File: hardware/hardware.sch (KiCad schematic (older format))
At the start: 8 parts

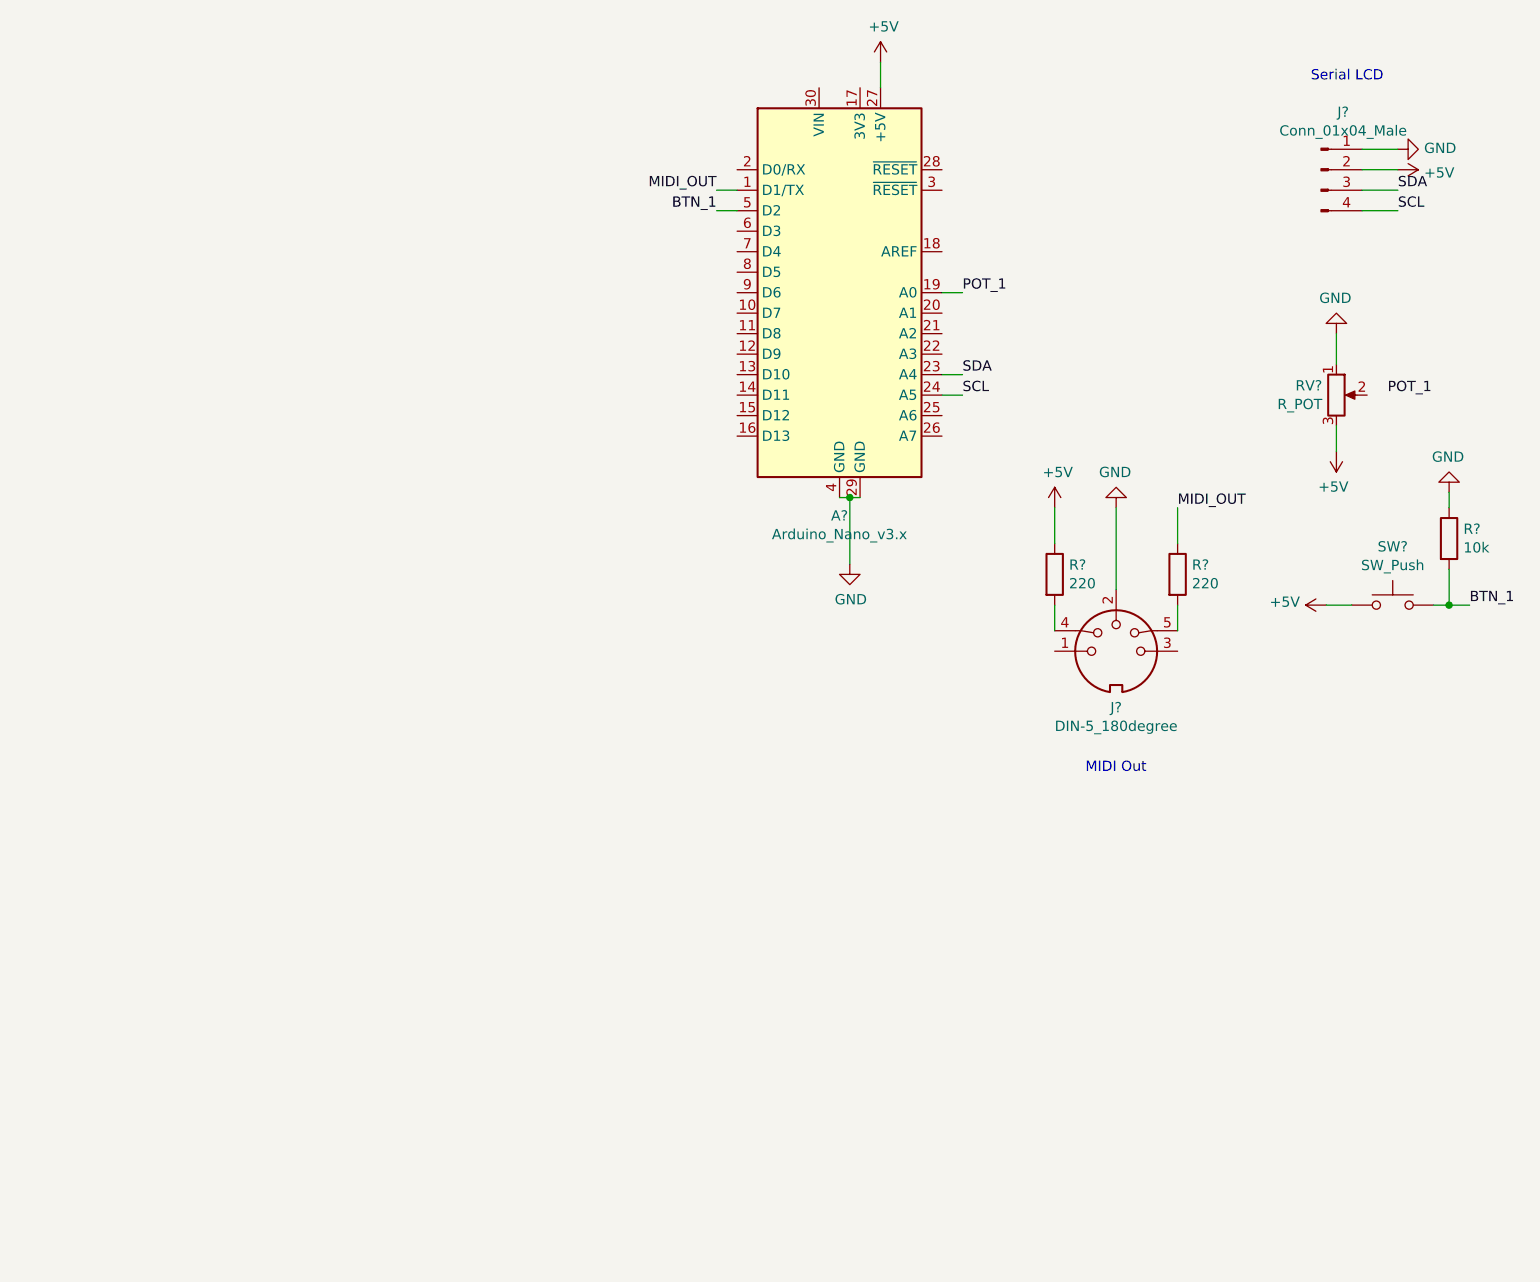
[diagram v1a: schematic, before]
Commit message: update schematic and add todo
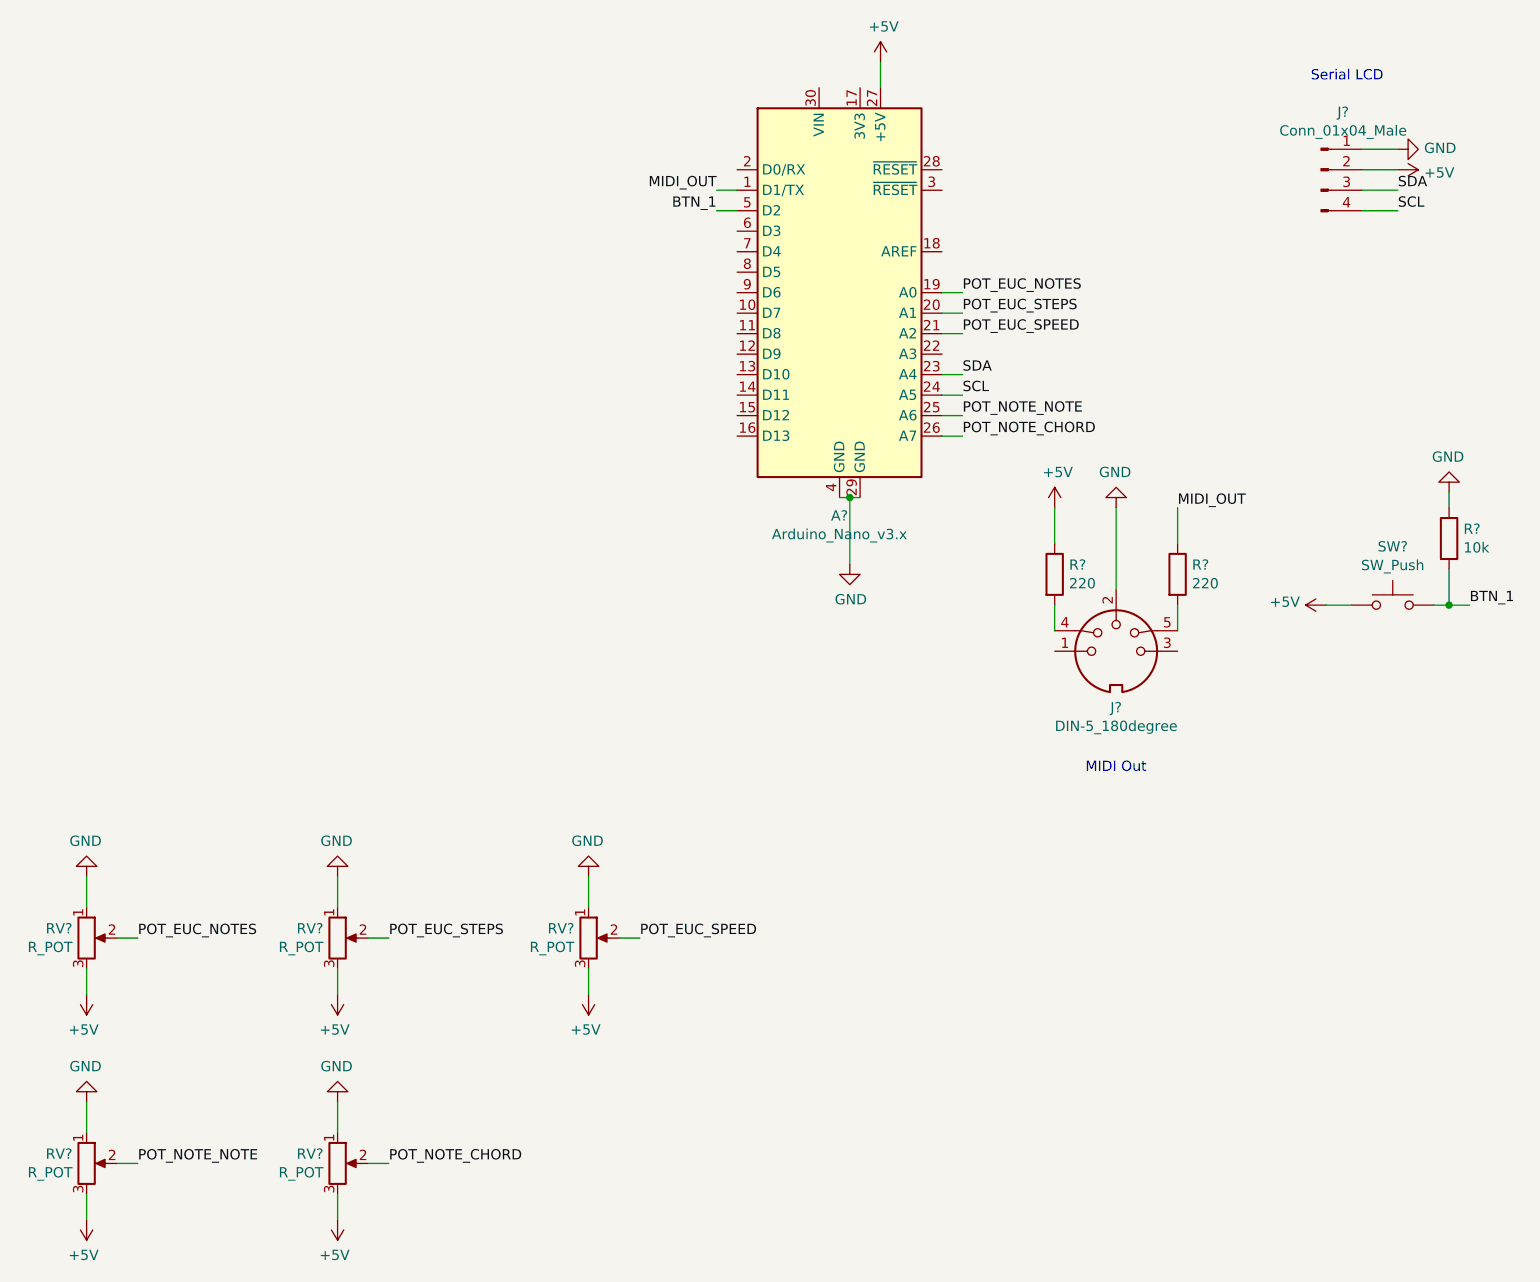
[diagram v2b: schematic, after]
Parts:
- added RV? (x4): R_POT, symbol Device:R_POT
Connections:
- net POT_1 is gone; now on net POT_EUC_NOTES: A?.19 (A0)
- net +5V: now also RV?.3, RV?.3, RV?.3, RV?.3
- net GND: now also RV?.1, RV?.1, RV?.1, RV?.1
- net POT_EUC_STEPS: now reaches A?.20 (A1)
- net POT_EUC_STEPS: now also RV?.2
- net POT_EUC_SPEED: now reaches A?.21 (A2)
- net POT_EUC_SPEED: now also RV?.2
- net POT_NOTE_NOTE: now reaches A?.25 (A6)
- net POT_NOTE_NOTE: now also RV?.2
- net POT_NOTE_CHORD: now reaches A?.26 (A7)
- net POT_NOTE_CHORD: now also RV?.2
- net POT_EUC_NOTES: now reaches RV?.2
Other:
- moved on the sheet: RV?
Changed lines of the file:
@@
 L Device:R_POT RV?
 U 1 1 5FC51EFD
-P 7500 3250
-F 0 "RV?" H 7431 3296 50  0000 R CNN
-F 1 "R_POT" H 7431 3205 50  0000 R CNN
-F 2 "" H 7500 3250 50  0001 C CNN
-F 3 "~" H 7500 3250 50  0001 C CNN
-	1    7500 3250
+P 1400 5900
+F 0 "RV?" H 1331 5946 50  0000 R CNN
+F 1 "R_POT" H 1331 5855 50  0000 R CNN
+F 2 "" H 1400 5900 50  0001 C CNN
+F 3 "~" H 1400 5900 50  0001 C CNN
+	1    1400 5900
 	1    0    0    -1
 $EndComp
@@
 	4475 2250 4575 2250
 Text Label 5675 2750 0    50   ~ 0
-POT_1
+POT_EUC_NOTES
 Text Label 4475 2350 2    50   ~ 0
 BTN_1
@@
 L power:GND #PWR?
 U 1 1 5FC5C0D4
-P 7500 2950
-F 0 "#PWR?" H 7500 2700 50  0001 C CNN
-F 1 "GND" H 7505 2777 50  0000 C CNN
-F 2 "" H 7500 2950 50  0001 C CNN
-F 3 "" H 7500 2950 50  0001 C CNN
-	1    7500 2950
+P 1400 5600
+F 0 "#PWR?" H 1400 5350 50  0001 C CNN
+F 1 "GND" H 1405 5427 50  0000 C CNN
+F 2 "" H 1400 5600 50  0001 C CNN
+F 3 "" H 1400 5600 50  0001 C CNN
+	1    1400 5600
 	-1   0    0    1
 $EndComp
@@
 L power:+5V #PWR?
 U 1 1 5FC5C2F2
-P 7500 3525
-F 0 "#PWR?" H 7500 3375 50  0001 C CNN
-F 1 "+5V" H 7515 3698 50  0000 C CNN
-F 2 "" H 7500 3525 50  0001 C CNN
-F 3 "" H 7500 3525 50  0001 C CNN
-	1    7500 3525
-	-1   0    0    1
-$EndComp
-Wire Wire Line
-	7500 2950 7500 3100
-Wire Wire Line
-	7500 3400 7500 3525
-Text Label 7750 3250 0    50   ~ 0
-POT_1
+P 1400 6175
+F 0 "#PWR?" H 1400 6025 50  0001 C CNN
+F 1 "+5V" H 1415 6348 50  0000 C CNN
+F 2 "" H 1400 6175 50  0001 C CNN
+F 3 "" H 1400 6175 50  0001 C CNN
+	1    1400 6175
+	-1   0    0    1
+$EndComp
+Wire Wire Line
+	1400 5600 1400 5750
+Wire Wire Line
+	1400 6050 1400 6175
+Text Label 1650 5900 0    50   ~ 0
+POT_EUC_NOTES
 Text Label 8150 4275 0    50   ~ 0
 BTN_1
@@
 Wire Wire Line
 	8050 4275 8150 4275
+$Comp
+L Device:R_POT RV?
+U 1 1 5FCA6913
+P 2625 5900
+F 0 "RV?" H 2556 5946 50  0000 R CNN
+F 1 "R_POT" H 2556 5855 50  0000 R CNN
+F 2 "" H 2625 5900 50  0001 C CNN
+F 3 "~" H 2625 5900 50  0001 C CNN
+	1    2625 5900
+	1    0    0    -1
+$EndComp
+$Comp
+L power:GND #PWR?
+U 1 1 5FCA6919
+P 2625 5600
+F 0 "#PWR?" H 2625 5350 50  0001 C CNN
+F 1 "GND" H 2630 5427 50  0000 C CNN
+F 2 "" H 2625 5600 50  0001 C CNN
+F 3 "" H 2625 5600 50  0001 C CNN
+	1    2625 5600
+	-1   0    0    1
+$EndComp
+$Comp
+L power:+5V #PWR?
+U 1 1 5FCA691F
+P 2625 6175
+F 0 "#PWR?" H 2625 6025 50  0001 C CNN
+F 1 "+5V" H 2640 6348 50  0000 C CNN
+F 2 "" H 2625 6175 50  0001 C CNN
+F 3 "" H 2625 6175 50  0001 C CNN
+	1    2625 6175
+	-1   0    0    1
+$EndComp
+Wire Wire Line
+	2625 5600 2625 5750
+Wire Wire Line
+	2625 6050 2625 6175
+Text Label 2875 5900 0    50   ~ 0
+POT_EUC_STEPS
+Text Label 5675 2850 0    50   ~ 0
+POT_EUC_STEPS
+Wire Wire Line
+	5675 2850 5575 2850
+$Comp
+L Device:R_POT RV?
+U 1 1 5FCA7C9D
+P 3850 5900
+F 0 "RV?" H 3781 5946 50  0000 R CNN
+F 1 "R_POT" H 3781 5855 50  0000 R CNN
+F 2 "" H 3850 5900 50  0001 C CNN
+F 3 "~" H 3850 5900 50  0001 C CNN
+	1    3850 5900
+	1    0    0    -1
+$EndComp
+$Comp
+L power:GND #PWR?
+U 1 1 5FCA7CA3
+P 3850 5600
+F 0 "#PWR?" H 3850 5350 50  0001 C CNN
+F 1 "GND" H 3855 5427 50  0000 C CNN
+F 2 "" H 3850 5600 50  0001 C CNN
+F 3 "" H 3850 5600 50  0001 C CNN
+	1    3850 5600
+	-1   0    0    1
+$EndComp
+$Comp
+L power:+5V #PWR?
+U 1 1 5FCA7CA9
+P 3850 6175
+F 0 "#PWR?" H 3850 6025 50  0001 C CNN
+F 1 "+5V" H 3865 6348 50  0000 C CNN
+F 2 "" H 3850 6175 50  0001 C CNN
+F 3 "" H 3850 6175 50  0001 C CNN
+	1    3850 6175
+	-1   0    0    1
+$EndComp
+Text Label 4100 5900 0    50   ~ 0
+POT_EUC_SPEED
+Wire Wire Line
+	3850 5600 3850 5750
+Wire Wire Line
+	3850 6175 3850 6050
+Wire Wire Line
+	4000 5900 4100 5900
+Text Label 5675 2950 0    50   ~ 0
+POT_EUC_SPEED
+Wire Wire Line
+	5575 2950 5675 2950
+$Comp
+L Device:R_POT RV?
+U 1 1 5FCAA5E5
+P 1400 7000
+F 0 "RV?" H 1331 7046 50  0000 R CNN
+F 1 "R_POT" H 1331 6955 50  0000 R CNN
+F 2 "" H 1400 7000 50  0001 C CNN
+F 3 "~" H 1400 7000 50  0001 C CNN
+	1    1400 7000
+	1    0    0    -1
+$EndComp
+$Comp
+L power:GND #PWR?
+U 1 1 5FCAA5EB
+P 1400 6700
+F 0 "#PWR?" H 1400 6450 50  0001 C CNN
+F 1 "GND" H 1405 6527 50  0000 C CNN
+F 2 "" H 1400 6700 50  0001 C CNN
+F 3 "" H 1400 6700 50  0001 C CNN
+	1    1400 6700
+	-1   0    0    1
+$EndComp
+$Comp
+L power:+5V #PWR?
+U 1 1 5FCAA5F1
+P 1400 7275
+F 0 "#PWR?" H 1400 7125 50  0001 C CNN
+F 1 "+5V" H 1415 7448 50  0000 C CNN
+F 2 "" H 1400 7275 50  0001 C CNN
+F 3 "" H 1400 7275 50  0001 C CNN
+	1    1400 7275
+	-1   0    0    1
+$EndComp
+Text Label 1650 7000 0    50   ~ 0
+POT_NOTE_NOTE
+Wire Wire Line
+	1400 6700 1400 6850
+Wire Wire Line
+	1400 7275 1400 7150
+Wire Wire Line
+	1550 7000 1650 7000
+$Comp
+L Device:R_POT RV?
+U 1 1 5FCAB786
+P 2625 7000
+F 0 "RV?" H 2556 7046 50  0000 R CNN
+F 1 "R_POT" H 2556 6955 50  0000 R CNN
+F 2 "" H 2625 7000 50  0001 C CNN
+F 3 "~" H 2625 7000 50  0001 C CNN
+	1    2625 7000
+	1    0    0    -1
+$EndComp
+$Comp
+L power:GND #PWR?
+U 1 1 5FCAB78C
+P 2625 6700
+F 0 "#PWR?" H 2625 6450 50  0001 C CNN
+F 1 "GND" H 2630 6527 50  0000 C CNN
+F 2 "" H 2625 6700 50  0001 C CNN
+F 3 "" H 2625 6700 50  0001 C CNN
+	1    2625 6700
+	-1   0    0    1
+$EndComp
+$Comp
+L power:+5V #PWR?
+U 1 1 5FCAB792
+P 2625 7275
+F 0 "#PWR?" H 2625 7125 50  0001 C CNN
+F 1 "+5V" H 2640 7448 50  0000 C CNN
+F 2 "" H 2625 7275 50  0001 C CNN
+F 3 "" H 2625 7275 50  0001 C CNN
+	1    2625 7275
+	-1   0    0    1
+$EndComp
+Text Label 2875 7000 0    50   ~ 0
+POT_NOTE_CHORD
+Wire Wire Line
+	2625 6700 2625 6850
+Wire Wire Line
+	2625 7275 2625 7150
+Wire Wire Line
+	2775 7000 2875 7000
+Wire Wire Line
+	1550 5900 1650 5900
+Wire Wire Line
+	2875 5900 2775 5900
+Text Label 5675 3350 0    50   ~ 0
+POT_NOTE_NOTE
+Text Label 5675 3450 0    50   ~ 0
+POT_NOTE_CHORD
+Wire Wire Line
+	5575 3350 5675 3350
+Wire Wire Line
+	5675 3450 5575 3450
 $EndSCHEMATC

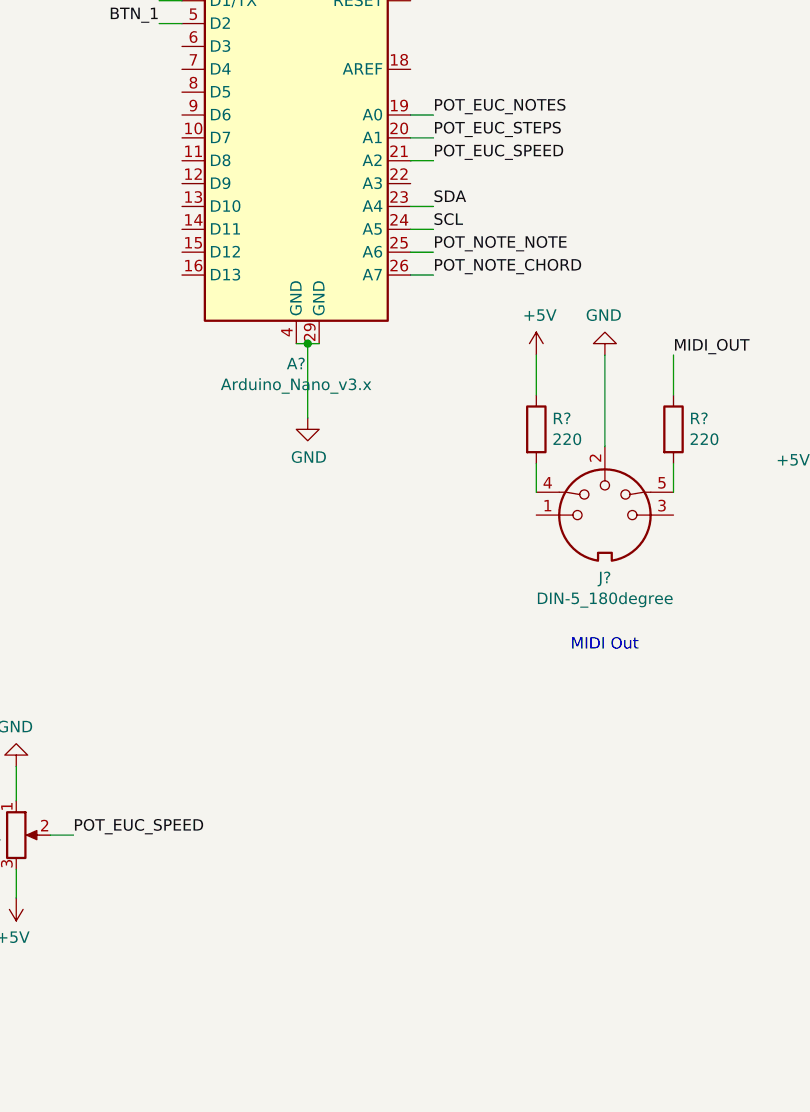
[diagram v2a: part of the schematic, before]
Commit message: Assign pot pins
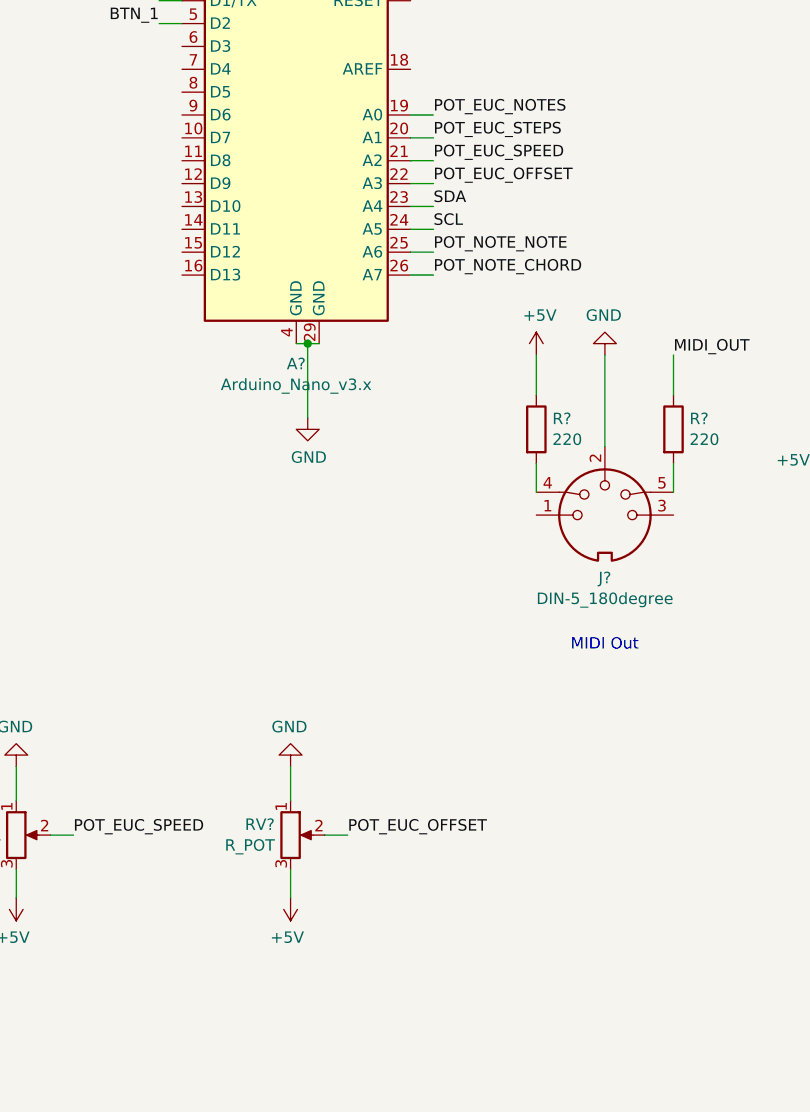
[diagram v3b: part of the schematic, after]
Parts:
- added RV?: R_POT, symbol Device:R_POT
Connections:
- net +5V: now also RV?.3
- net GND: now also RV?.1
- net POT_EUC_OFFSET: now reaches A?.22 (A3)
- net POT_EUC_OFFSET: now also RV?.2
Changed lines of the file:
@@
 Wire Wire Line
 	5675 3450 5575 3450
+$Comp
+L Device:R_POT RV?
+U 1 1 5FCB031C
+P 5050 5900
+F 0 "RV?" H 4981 5946 50  0000 R CNN
+F 1 "R_POT" H 4981 5855 50  0000 R CNN
+F 2 "" H 5050 5900 50  0001 C CNN
+F 3 "~" H 5050 5900 50  0001 C CNN
+	1    5050 5900
+	1    0    0    -1
+$EndComp
+$Comp
+L power:GND #PWR?
+U 1 1 5FCB0322
+P 5050 5600
+F 0 "#PWR?" H 5050 5350 50  0001 C CNN
+F 1 "GND" H 5055 5427 50  0000 C CNN
+F 2 "" H 5050 5600 50  0001 C CNN
+F 3 "" H 5050 5600 50  0001 C CNN
+	1    5050 5600
+	-1   0    0    1
+$EndComp
+$Comp
+L power:+5V #PWR?
+U 1 1 5FCB0328
+P 5050 6175
+F 0 "#PWR?" H 5050 6025 50  0001 C CNN
+F 1 "+5V" H 5065 6348 50  0000 C CNN
+F 2 "" H 5050 6175 50  0001 C CNN
+F 3 "" H 5050 6175 50  0001 C CNN
+	1    5050 6175
+	-1   0    0    1
+$EndComp
+Text Label 5300 5900 0    50   ~ 0
+POT_EUC_OFFSET
+Wire Wire Line
+	5050 5600 5050 5750
+Wire Wire Line
+	5050 6175 5050 6050
+Wire Wire Line
+	5200 5900 5300 5900
+Text Label 5675 3050 0    50   ~ 0
+POT_EUC_OFFSET
+Wire Wire Line
+	5675 3050 5575 3050
 $EndSCHEMATC
